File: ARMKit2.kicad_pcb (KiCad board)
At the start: 2 copper layers, 40 parts, among them P1 CONN_01X06, P2 CONN_01X32, P3 CONN_01X32, P4 USB_B, U1 STM32F405RG, U2 LT1761, Y1 Crystal, Y2 Crystal

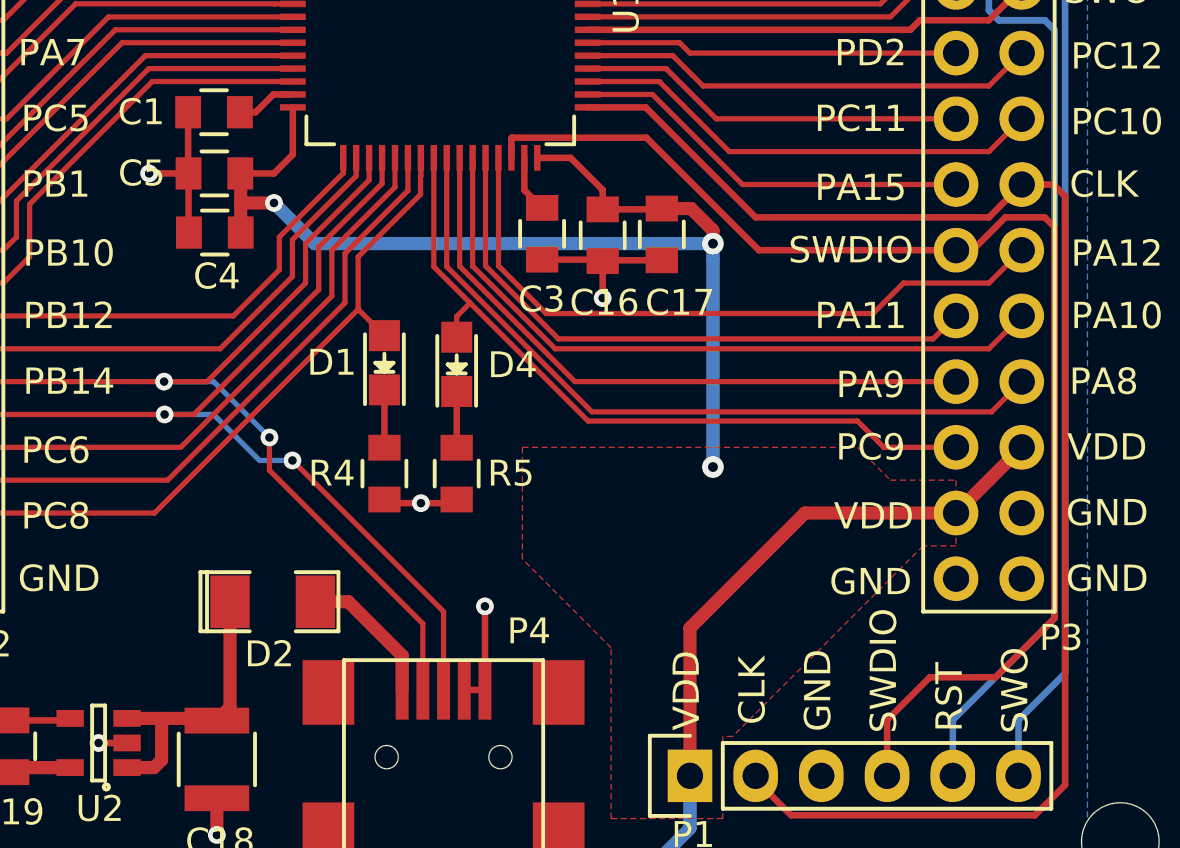
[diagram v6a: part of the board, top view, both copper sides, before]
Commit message: Moved USB to PA11/PA12
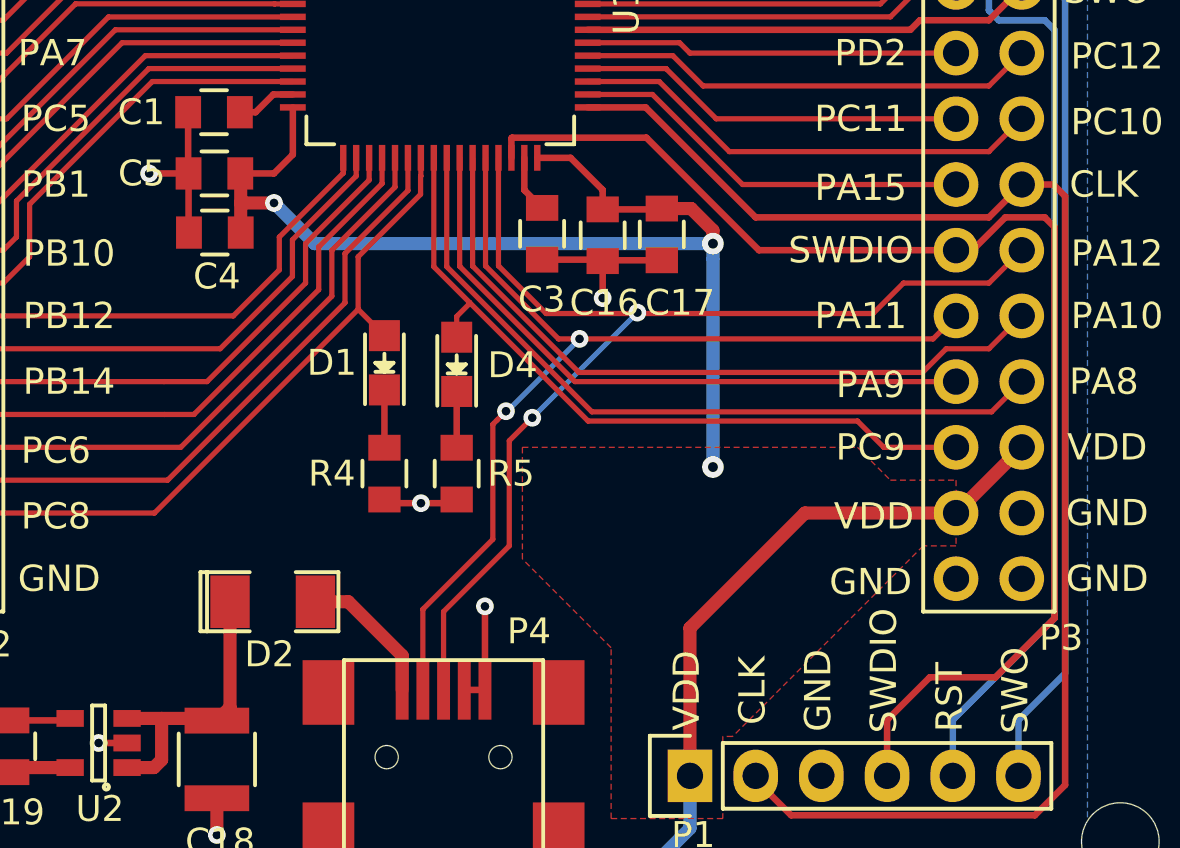
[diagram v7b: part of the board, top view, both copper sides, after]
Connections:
- P4 pad 2: PB14 -> PA11
- P4 pad 3: PB15 -> PA12
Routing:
- net PA12: track 26.2 -> 43.9 mm, vias 0 -> 2
- net PB14: track 37.6 -> 20.4 mm, vias 2 -> 0
- net PB15: track 41.6 -> 24.6 mm, vias 2 -> 0
- net PA11: track 23.9 -> 40.1 mm, vias 0 -> 2
- net PA10: track 27.3 -> 28.0 mm
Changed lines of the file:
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@@
   (general
     (links 140)
-    (no_connects 0)
-    (area 44.359074 80.477099 110.042446 143.08866)
+    (no_connects 2)
+    (area 0 0 0 0)
     (thickness 1.6)
     (drawings 75)
-    (tracks 529)
+    (tracks 534)
     (zones 0)
     (modules 40)
@@
       (net 14 "Net-(D2-Pad2)") (solder_mask_margin 0.0508))
     (pad 2 smd rect (at 3.44932 -0.8001 90) (size 2.30124 0.50038) (layers F.Cu F.Paste F.Mask)
-      (net 60 PB14) (solder_mask_margin 0.0508))
+      (net 51 PA11) (solder_mask_margin 0.0508))
     (pad 3 smd rect (at 3.44932 0 90) (size 2.30124 0.50038) (layers F.Cu F.Paste F.Mask)
-      (net 59 PB15) (solder_mask_margin 0.0508))
+      (net 50 PA12) (solder_mask_margin 0.0508))
     (pad 4 smd rect (at 3.44932 0.8001 90) (size 2.30124 0.50038) (layers F.Cu F.Paste F.Mask)
       (net 1 GND) (solder_mask_margin 0.0508))
@@
   (segment (start 83.514 108.279) (end 86.995 111.76) (width 0.2032) (layer F.Cu) (net 49))
   (segment (start 81.011 108.279) (end 83.514 108.279) (width 0.2032) (layer F.Cu) (net 49))
+  (segment (start 77.978 121.666) (end 78.867 120.777) (width 0.2032) (layer F.Cu) (net 50))
+  (segment (start 78.867 120.776976) (end 78.867 120.777) (width 0.2032) (layer B.Cu) (net 50))
+  (segment (start 82.930976 116.713) (end 78.867 120.776976) (width 0.2032) (layer B.Cu) (net 50))
+  (via (at 78.867 120.777) (size 0.6858) (drill 0.3302) (layers F.Cu B.Cu) (net 50))
+  (via (at 82.930976 116.713) (size 0.6858) (drill 0.3302) (layers F.Cu B.Cu) (net 50))
+  (segment (start 77.978 125.73) (end 75.438 128.27) (width 0.2032) (layer F.Cu) (net 50))
+  (segment (start 75.438 128.27) (end 75.438 131.29768) (width 0.2032) (layer F.Cu) (net 50))
+  (segment (start 77.978 121.666) (end 77.978 125.73) (width 0.2032) (layer F.Cu) (net 50))
+  (segment (start 81.145743 116.747133) (end 92.040867 116.747133) (width 0.2032) (layer F.Cu) (net 50))
+  (segment (start 79.404041 116.747133) (end 81.145743 116.747133) (width 0.2032) (layer F.Cu) (net 50))
   (segment (start 93.218 115.57) (end 96.52 115.57) (width 0.2032) (layer F.Cu) (net 50))
   (segment (start 96.52 115.57) (end 97.79 114.3) (width 0.2032) (layer F.Cu) (net 50))
   (segment (start 92.040867 116.747133) (end 93.218 115.57) (width 0.2032) (layer F.Cu) (net 50))
   (segment (start 77.561 114.904092) (end 79.404041 116.747133) (width 0.2032) (layer F.Cu) (net 50))
-  (segment (start 79.404041 116.747133) (end 92.040867 116.747133) (width 0.2032) (layer F.Cu) (net 50))
   (segment (start 77.561 110.729) (end 77.561 114.904092) (width 0.2032) (layer F.Cu) (net 50))
+  (segment (start 77.343 121.031) (end 77.508101 120.865899) (width 0.2032) (layer F.Cu) (net 51))
+  (segment (start 77.343 125.476) (end 77.343 121.031) (width 0.2032) (layer F.Cu) (net 51))
+  (segment (start 74.6379 128.1811) (end 77.343 125.476) (width 0.2032) (layer F.Cu) (net 51))
+  (segment (start 77.508101 120.865899) (end 77.851 120.523) (width 0.2032) (layer F.Cu) (net 51))
+  (segment (start 74.6379 131.29768) (end 74.6379 128.1811) (width 0.2032) (layer F.Cu) (net 51))
+  (segment (start 77.90112 120.523) (end 77.851 120.523) (width 0.2032) (layer B.Cu) (net 51))
+  (segment (start 80.69512 117.729) (end 77.90112 120.523) (width 0.2032) (layer B.Cu) (net 51))
+  (via (at 77.851 120.523) (size 0.6858) (drill 0.3302) (layers F.Cu B.Cu) (net 51))
+  (segment (start 80.69512 117.729) (end 94.361 117.729) (width 0.2032) (layer F.Cu) (net 51))
+  (via (at 80.69512 117.729) (size 0.6858) (drill 0.3302) (layers F.Cu B.Cu) (net 51))
+  (segment (start 79.883 117.729) (end 80.69512 117.729) (width 0.2032) (layer F.Cu) (net 51))
   (segment (start 77.061 110.729) (end 77.061 114.907) (width 0.2032) (layer F.Cu) (net 51))
   (segment (start 77.061 114.907) (end 79.883 117.729) (width 0.2032) (layer F.Cu) (net 51))
-  (segment (start 79.883 117.729) (end 94.361 117.729) (width 0.2032) (layer F.Cu) (net 51))
   (segment (start 94.361 117.729) (end 95.25 116.84) (width 0.2032) (layer F.Cu) (net 51))
-  (segment (start 76.561 110.729) (end 76.561 114.915) (width 0.2032) (layer F.Cu) (net 52))
-  (segment (start 76.561 114.915) (end 79.756 118.11) (width 0.2032) (layer F.Cu) (net 52))
-  (segment (start 79.756 118.11) (end 96.52 118.11) (width 0.2032) (layer F.Cu) (net 52))
-  (segment (start 96.52 118.11) (end 97.79 116.84) (width 0.2032) (layer F.Cu) (net 52))
+  (segment (start 74.676 131.25958) (end 74.6379 131.29768) (width 0.2032) (layer F.Cu) (net 51))
+  (segment (start 97.79 116.84) (end 96.52 118.11) (width 0.2032) (layer F.Cu) (net 52))
+  (segment (start 96.52 118.11) (end 94.86595 118.11) (width 0.2032) (layer F.Cu) (net 52))
+  (segment (start 94.86595 118.11) (end 93.95156 119.02439) (width 0.2032) (layer F.Cu) (net 52))
+  (segment (start 93.95156 119.02439) (end 80.67039 119.02439) (width 0.2032) (layer F.Cu) (net 52))
+  (segment (start 80.67039 119.02439) (end 76.561 114.915) (width 0.2032) (layer F.Cu) (net 52))
+  (segment (start 76.561 114.915) (end 76.561 110.729) (width 0.2032) (layer F.Cu) (net 52))
   (segment (start 76.061 110.729) (end 76.061 114.923) (width 0.2032) (layer F.Cu) (net 53))
   (segment (start 76.061 114.923) (end 80.518 119.38) (width 0.2032) (layer F.Cu) (net 53))
@@
   (segment (start 73.561 111.859) (end 71.12 114.3) (width 0.2032) (layer F.Cu) (net 58))
   (segment (start 73.561 110.729) (end 73.561 111.859) (width 0.2032) (layer F.Cu) (net 58))
-  (segment (start 75.438 131.29768) (end 75.438 128.27) (width 0.2032) (layer F.Cu) (net 59))
-  (segment (start 75.438 128.27) (end 69.596 122.428) (width 0.2032) (layer F.Cu) (net 59))
-  (segment (start 68.326 122.428) (end 69.596 122.428) (width 0.2032) (layer B.Cu) (net 59))
-  (via (at 69.596 122.428) (size 0.6858) (drill 0.3302) (layers F.Cu B.Cu) (net 59))
-  (segment (start 66.548 120.65) (end 68.326 122.428) (width 0.2032) (layer B.Cu) (net 59))
-  (segment (start 65.138717 120.65) (end 66.548 120.65) (width 0.2032) (layer B.Cu) (net 59))
-  (segment (start 64.653784 120.65) (end 65.138717 120.65) (width 0.2032) (layer B.Cu) (net 59))
   (segment (start 64.653784 120.65) (end 55.88 120.65) (width 0.2032) (layer F.Cu) (net 59))
   (segment (start 65.786 120.65) (end 64.653784 120.65) (width 0.2032) (layer F.Cu) (net 59))
-  (via (at 64.653784 120.65) (size 0.6858) (drill 0.3302) (layers F.Cu B.Cu) (net 59))
   (segment (start 73.061 110.729) (end 73.061 111.724) (width 0.2032) (layer F.Cu) (net 59))
   (segment (start 73.061 111.724) (end 70.612 114.173) (width 0.2032) (layer F.Cu) (net 59))
@@
   (segment (start 70.612 115.824) (end 65.786 120.65) (width 0.2032) (layer F.Cu) (net 59))
   (segment (start 55.88 120.65) (end 54.61 121.92) (width 0.2032) (layer F.Cu) (net 59))
-  (segment (start 74.6379 128.7399) (end 68.707 122.809) (width 0.2032) (layer F.Cu) (net 60))
-  (segment (start 68.707 122.809) (end 68.707 121.539) (width 0.2032) (layer F.Cu) (net 60))
-  (segment (start 74.6379 131.29768) (end 74.6379 128.7399) (width 0.2032) (layer F.Cu) (net 60))
-  (via (at 68.707 121.539) (size 0.6858) (drill 0.3302) (layers F.Cu B.Cu) (net 60))
-  (segment (start 66.548 119.38) (end 68.707 121.539) (width 0.2032) (layer B.Cu) (net 60))
-  (segment (start 65.118844 119.38) (end 66.548 119.38) (width 0.2032) (layer B.Cu) (net 60))
-  (segment (start 74.676 131.25958) (end 74.6379 131.29768) (width 0.2032) (layer F.Cu) (net 60))
-  (segment (start 64.633911 119.38) (end 65.118844 119.38) (width 0.2032) (layer B.Cu) (net 60))
   (segment (start 64.633911 119.38) (end 57.15 119.38) (width 0.2032) (layer F.Cu) (net 60))
   (segment (start 66.294 119.38) (end 64.633911 119.38) (width 0.2032) (layer F.Cu) (net 60))
-  (via (at 64.633911 119.38) (size 0.6858) (drill 0.3302) (layers F.Cu B.Cu) (net 60))
   (segment (start 72.561 110.729) (end 72.561 111.589) (width 0.2032) (layer F.Cu) (net 60))
   (segment (start 72.561 111.589) (end 70.104 114.046) (width 0.2032) (layer F.Cu) (net 60))

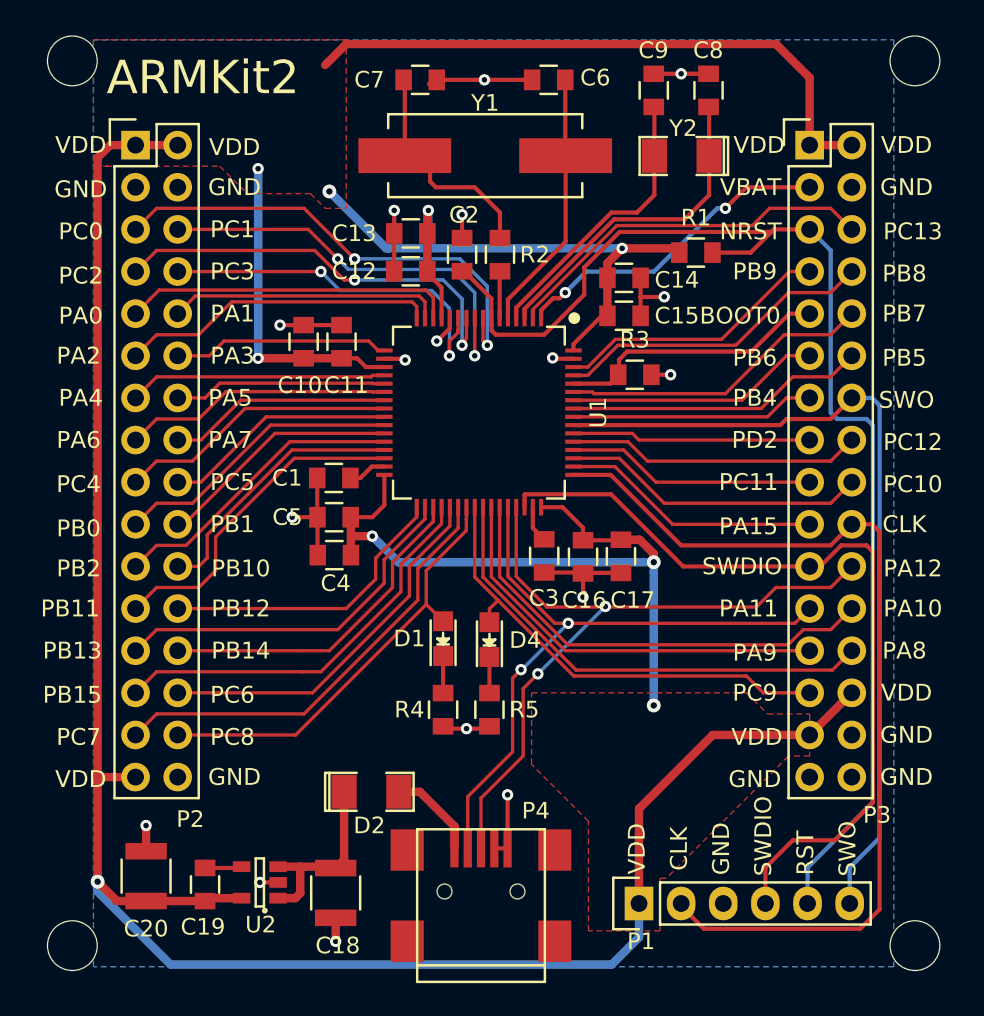
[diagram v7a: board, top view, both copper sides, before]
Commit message: Added BOOT and RESET buttons, much re-routing
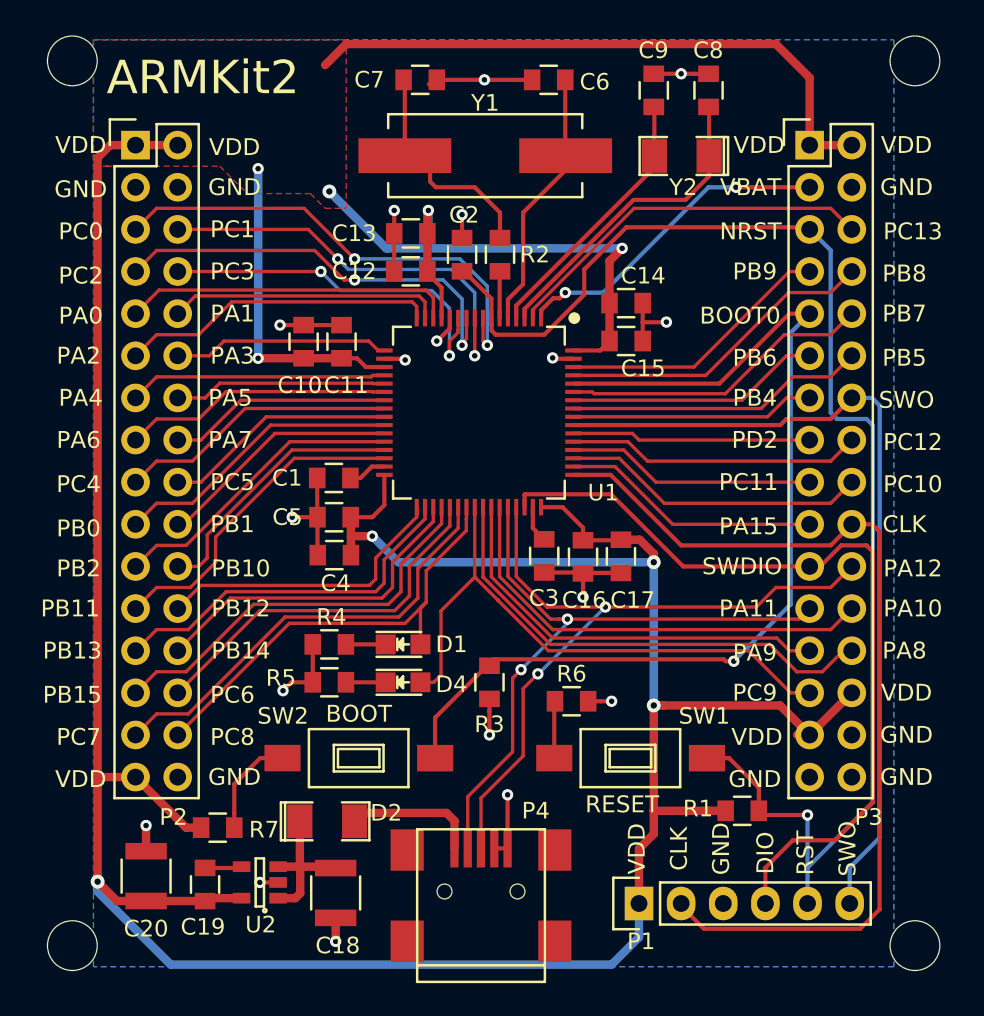
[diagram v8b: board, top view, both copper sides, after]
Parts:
- added R6: 1k, Capacitors_SMD:C_0805, F.Cu at (80.9, 122.4)
- added R7: 10k, Capacitors_SMD:C_0805, F.Cu at (59.6, 130.0)
- added SW1: SW_PUSH, Buttons_Switches_SMD:SW_SPST_FSMSM, F.Cu at (84.5, 125.9)
- added SW2: SW_PUSH, Buttons_Switches_SMD:SW_SPST_FSMSM, F.Cu at (68.1, 125.9)
- R3: value 0 -> 10k
- moved R1 33.8 mm to (91.2, 129.0), turned to 180 degrees
- moved R3 20.5 mm to (75.9, 121.3), turned to 270 degrees
- moved R5 9.79 mm to (66.3, 121.3), turned to 180 degrees
- moved R4 7.91 mm to (66.3, 119.0), turned to 180 degrees
- moved D4 5.81 mm to (70.7, 121.3), turned to 0 degrees
- moved D2 3.21 mm to (66.2, 129.7)
- moved D1 2.44 mm to (70.7, 119.0), turned to 0 degrees
- moved C14 1.53 mm to (84.2, 98.4)
- moved C15 1.53 mm to (84.2, 100.7)
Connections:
- R1 pad 1: VDD1 -> NRST
- R1 pad 2: NRST -> VDD1
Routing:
- net BOOT0: track 16.5 -> 61.0 mm, vias 0 -> 1
- net VDD1: track 258.3 -> 271.0 mm
- net NRST: track 76.5 -> 83.7 mm, vias 0 -> 1
- net PC9: track 28.8 -> 35.5 mm
- net Net-(R7-Pad1): track 0.00 -> 6.18 mm
- net GND: track 50.0 -> 53.8 mm, vias 17 -> 18
- net Net-(R6-Pad1): track 0.00 -> 3.45 mm
- net Net-(D2-Pad2): track 5.54 -> 8.09 mm
- net 5V_IN: track 11.4 -> 9.31 mm
- net PC8: track 26.5 -> 27.7 mm
- net OSC32_OUT: track 17.1 -> 16.2 mm
- net PA10: track 28.0 -> 27.3 mm
- net OSC32_IN: track 19.9 -> 19.2 mm
- net PA8: track 29.2 -> 29.8 mm
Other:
- board text added: "BOOT"
- board text added: "DIO"
- board text added: "RESET"
